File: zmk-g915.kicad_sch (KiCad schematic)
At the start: 43 parts, among them J3 Prog_conn, J5 Tag connect TC2030-CTX, SW2 Reset Switch, U3 nRF52840-QIAA-R/nRF52833-QIAA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, Y1 32MHz, Y2 32.768kHz

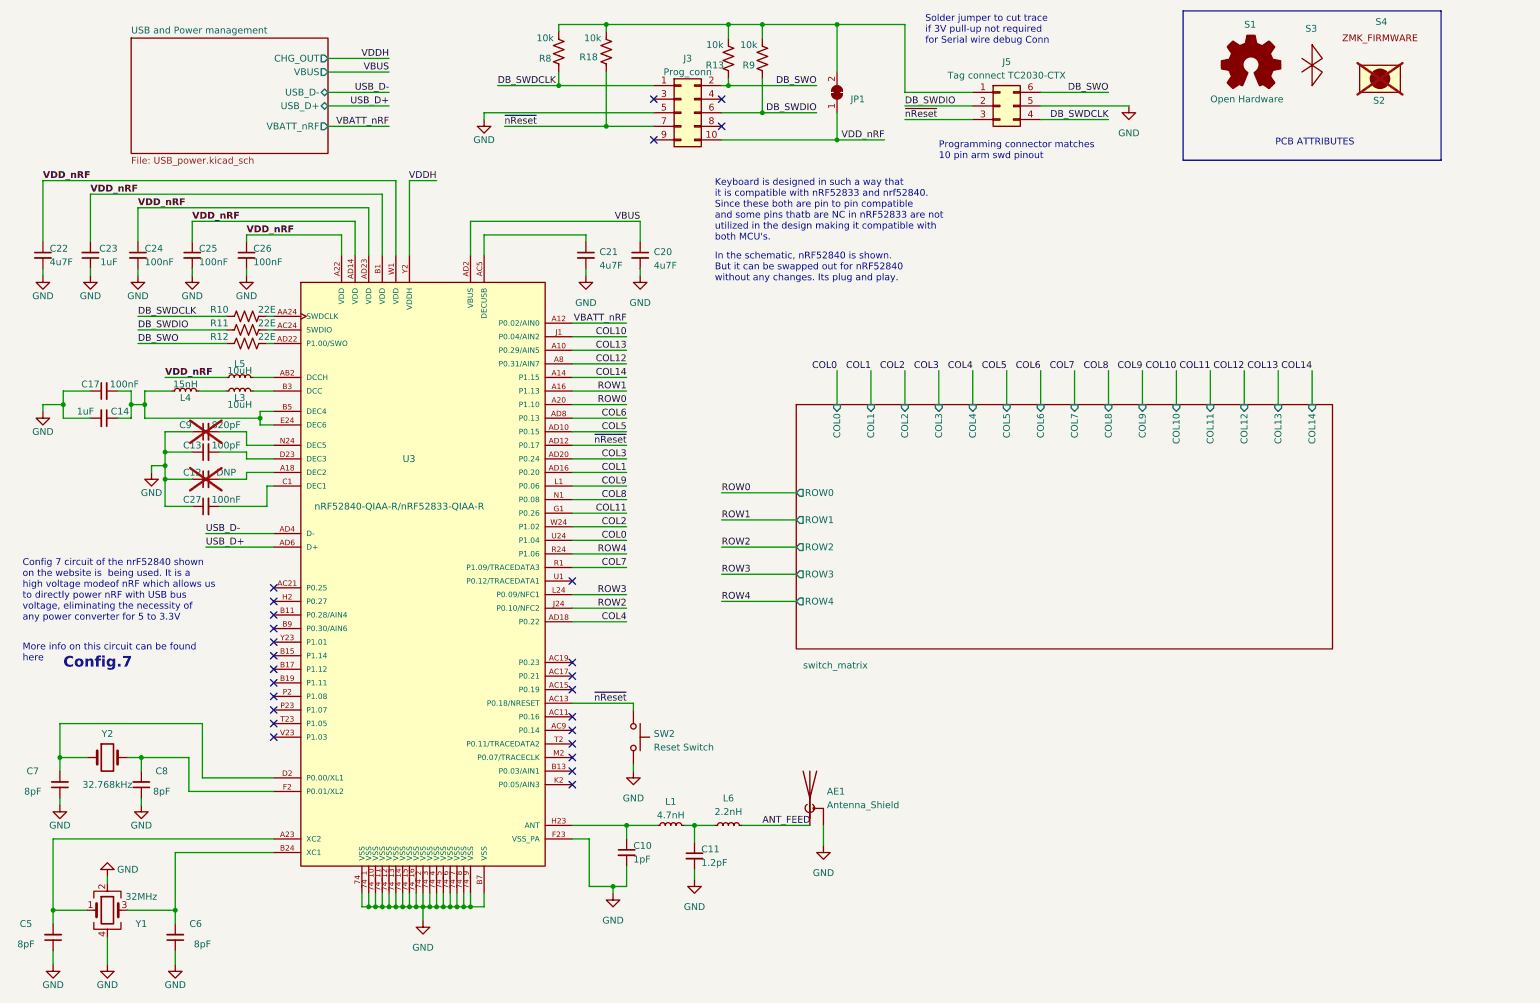
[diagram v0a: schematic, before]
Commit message: RGB and Keys added to sch
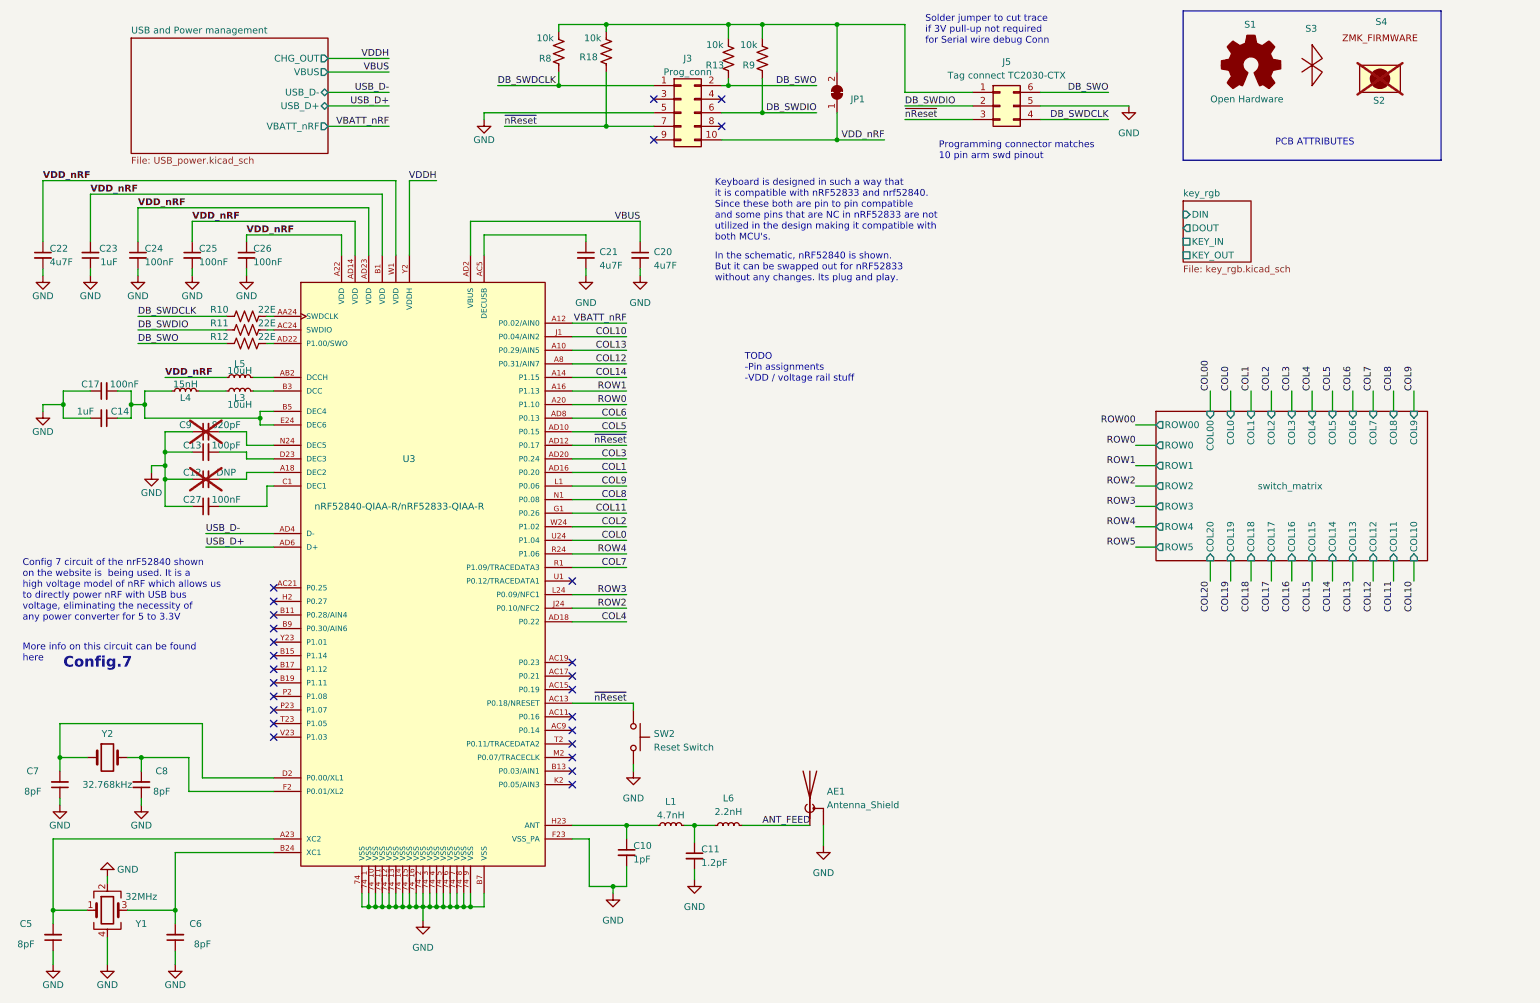
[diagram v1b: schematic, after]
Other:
- added sheet key_rgb (key_rgb.kicad_sch)
- sheet switch_matrix ports: added COL00, COL15, COL16, COL17, COL18, COL19, COL20, ROW00, ROW5; removed none
- note added: "Config 7 circuit of the nrF52840 shown on the website is being used. It is a high voltage model of nRF which allows us to directly power nRF with USB bus voltage, eliminating the necessity of any power converter for 5 to 3.3V"
- note added: "In the schematic, nRF52840 is shown. But it can be swapped out for nRF52833 without any changes. Its plug and play."
- note added: "Keyboard is designed in such a way that it is compatible with nRF52833 and nrf52840. Since these both are pin to pin compatible and some pins that are NC in nRF52833 are not utilized in the design making it compatible with both MCU's."
- note added: "TODO -Pin assignments -VDD / voltage rail stuff"
- note removed: "Config 7 circuit of the nrF52840 shown on the website is being used. It is a high voltage modeof nRF which allows us to directly power nRF with USB bus voltage, eliminating the necessity of any power converter for 5 to 3.3V"
- note removed: "In the schematic, nRF52840 is shown. But it can be swapped out for nRF52840 without any changes. Its plug and play."
- note removed: "Keyboard is designed in such a way that it is compatible with nRF52833 and nrf52840. Since these both are pin to pin compatible and some pins thatb are NC in nRF52833 are not utilized in the design making it compatible with both MCU's."

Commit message: Unified key sch pages
One large page is simpler in this case
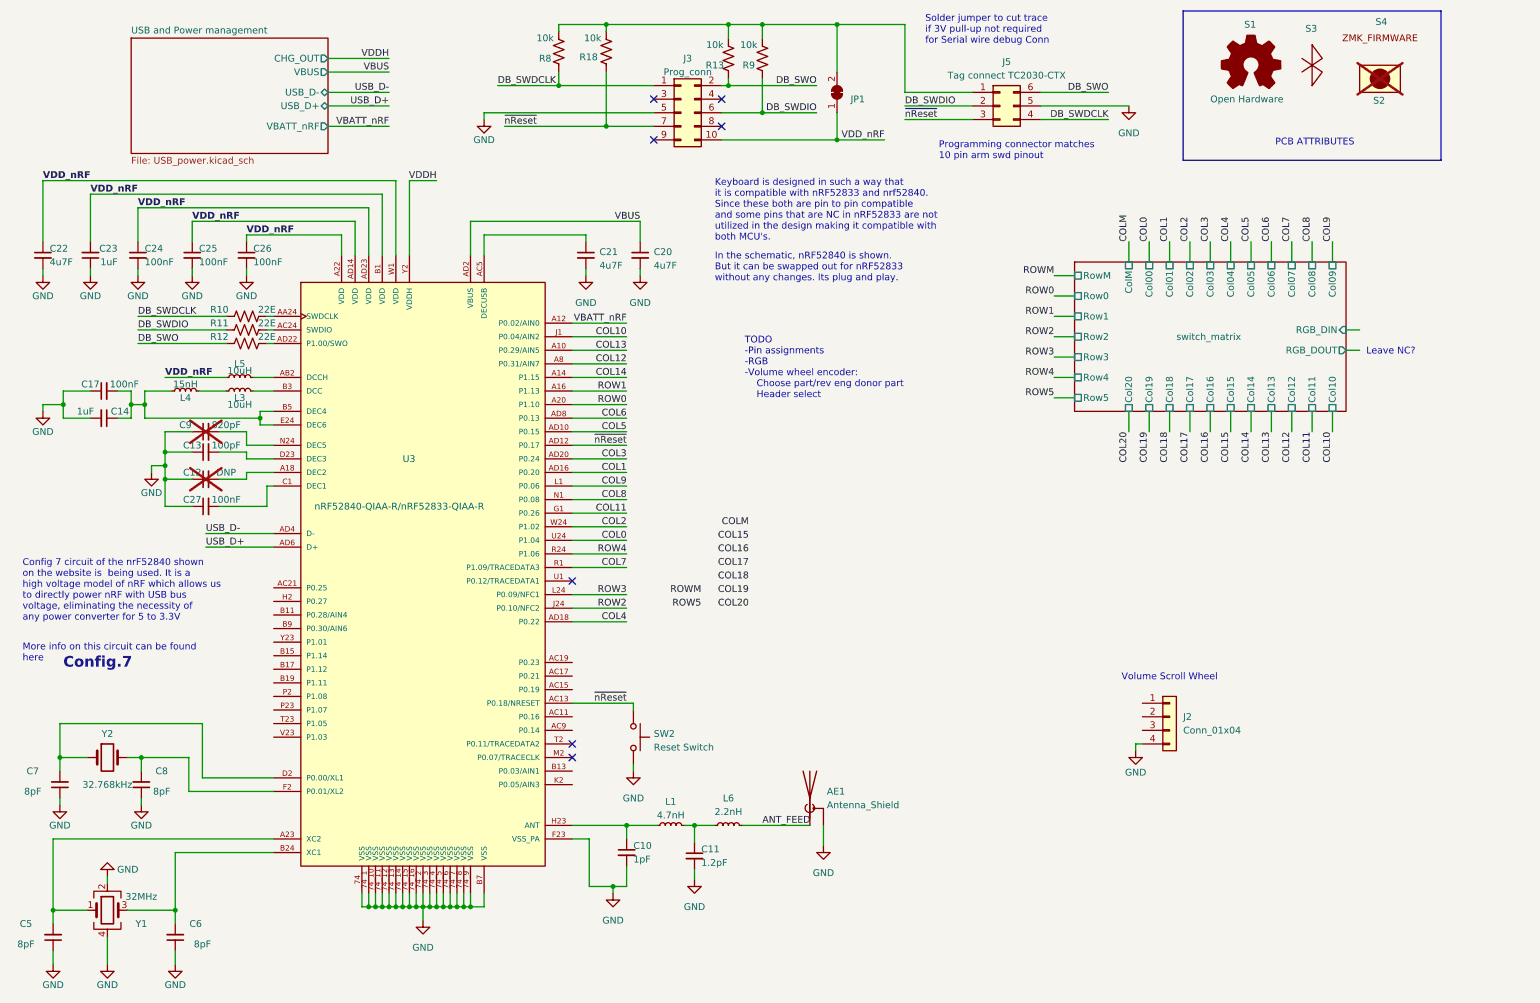
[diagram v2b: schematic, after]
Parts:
- added J2: Conn_01x04, symbol Connector_Generic:Conn_01x04
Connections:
- net GND: now also J2.4 (Pin_4)
- no-connect marks 26 -> 7
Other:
- removed sheet key_rgb
- sheet switch_matrix ports: added Col00, Col01, Col02, Col03, Col04, Col05, Col06, Col07, Col08, Col09, Col10, Col11, Col12, Col13, Col14, Col15, Col16, Col17, Col18, Col19, Col20, ColM, RGB_DIN, RGB_DOUT, Row0, Row1, Row2, Row3, Row4, Row5, RowM; removed COL0, COL00, COL1, COL10, COL11, COL12, COL13, COL14, COL15, COL16, COL17, COL18, COL19, COL2, COL20, COL3, COL4, COL5, COL6, COL7, COL8, COL9, ROW0, ROW00, ROW1, ROW2, ROW3, ROW4, ROW5
- note added: "Leave NC?"
- note added: "TODO -Pin assignments -RGB -Volume wheel encoder: Choose part/rev eng donor part Header select"
- note added: "Volume Scroll Wheel"
- note removed: "TODO -Pin assignments -VDD / voltage rail stuff"

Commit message: RGB LED level shifter. Various components
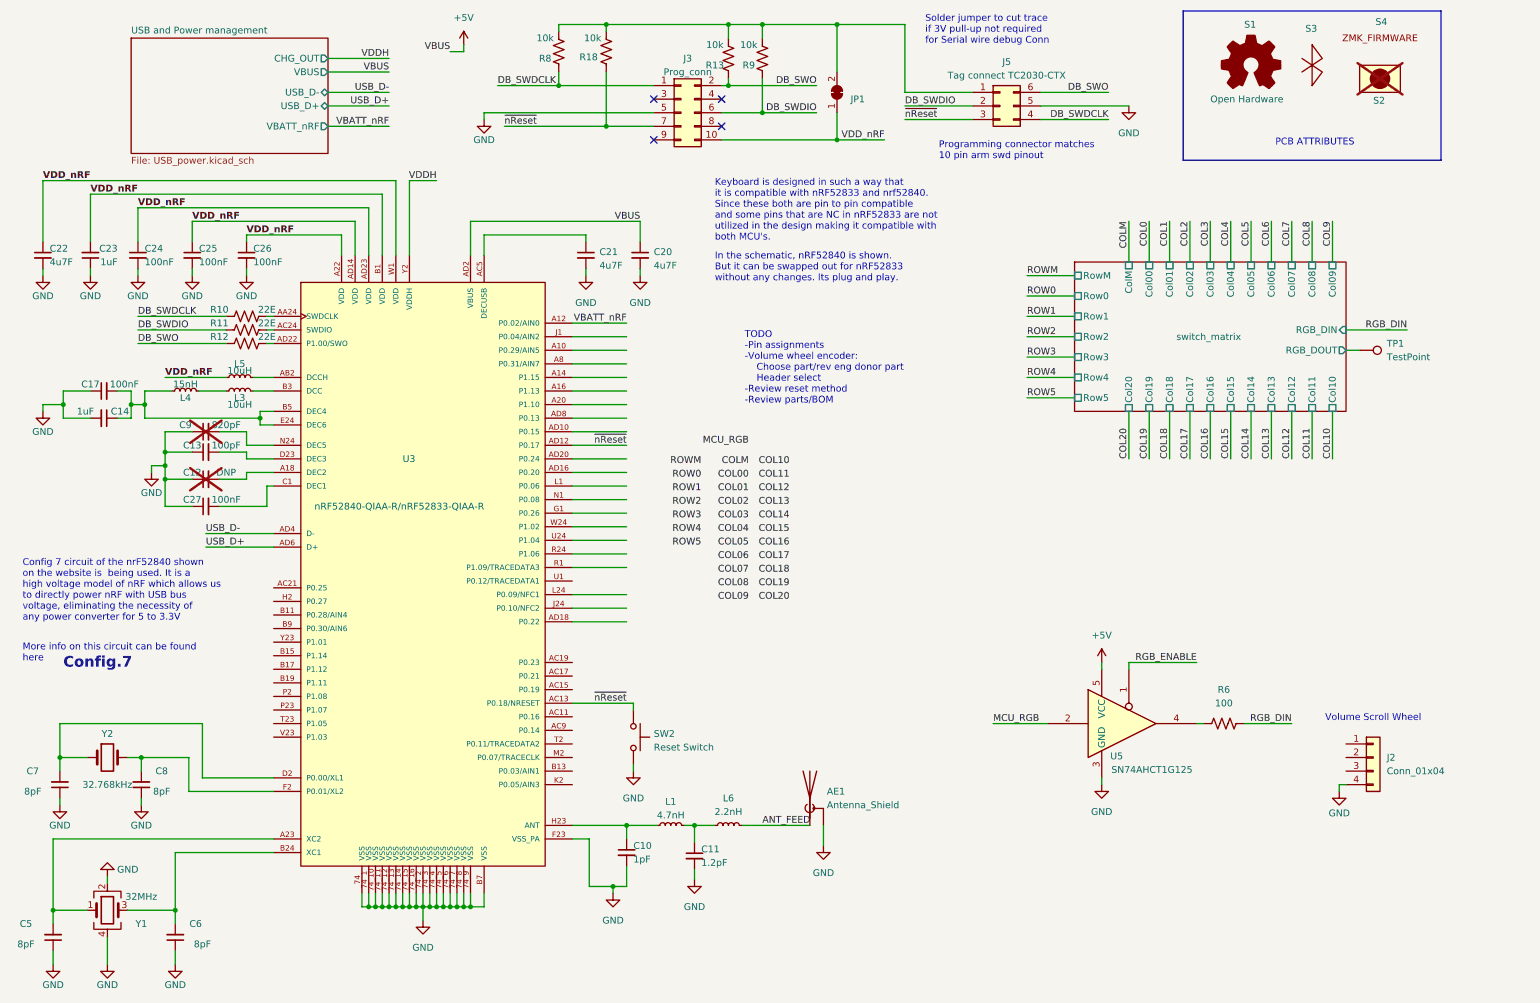
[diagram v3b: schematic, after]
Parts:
- added R6: 100, symbol Device:R_US
- added TP1: TestPoint, TestPoint:TestPoint_Pad_D1.5mm, symbol Connector:TestPoint
- added U5: SN74AHCT1G125, Package_TO_SOT_SMD:SOT-23-5, symbol 74xGxx:SN74LVC1G125DBV
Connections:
- net COL0: no longer U3.U24 (P1.04)
- net COL1: no longer U3.AD16 (P0.20)
- net COL10: no longer U3.J1 (P0.04/AIN2)
- net COL11: no longer U3.G1 (P0.26)
- net COL12: no longer U3.A8 (P0.31/AIN7)
- net COL13: no longer U3.A10 (P0.29/AIN5)
- net COL14: no longer U3.A14 (P1.15)
- net COL2: no longer U3.W24 (P1.02)
- net COL3: no longer U3.AD20 (P0.24)
- net COL4: no longer U3.AD18 (P0.22)
- net COL5: no longer U3.AD10 (P0.15)
- net COL6: no longer U3.AD8 (P0.13)
- net COL7: no longer U3.R1 (P1.09/TRACEDATA3)
- net COL8: no longer U3.N1 (P0.08)
- net COL9: no longer U3.L1 (P0.06)
- net GND: now also U5.3 (GND)
- net ROW0: no longer U3.A20 (P1.10)
- net ROW1: no longer U3.A16 (P1.13)
- net ROW2: no longer U3.J24 (P0.10/NFC2)
- net ROW3: no longer U3.L24 (P0.09/NFC1)
- net ROW4: no longer U3.R24 (P1.06)
- net switch_matrix/RGB_DOUT: now also TP1.1
- net VBUS renamed +5V
- net +5V: now also U5.5 (VCC)
- new net: R6.1, U5.4
- new net MCU_RGB: U5.2
- new net RGB_DIN: R6.2
- new net RGB_ENABLE: U5.1
- no-connect marks 7 -> 4
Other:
- note added: "TODO -Pin assignments -Volume wheel encoder: Choose part/rev eng donor part Header select -Review reset method -Review parts/BOM"
- note removed: "Leave NC?"
- note removed: "TODO -Pin assignments -RGB -Volume wheel encoder: Choose part/rev eng donor part Header select"
- moved on the sheet: J2

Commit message: Layout start. Add symbols to proj lib
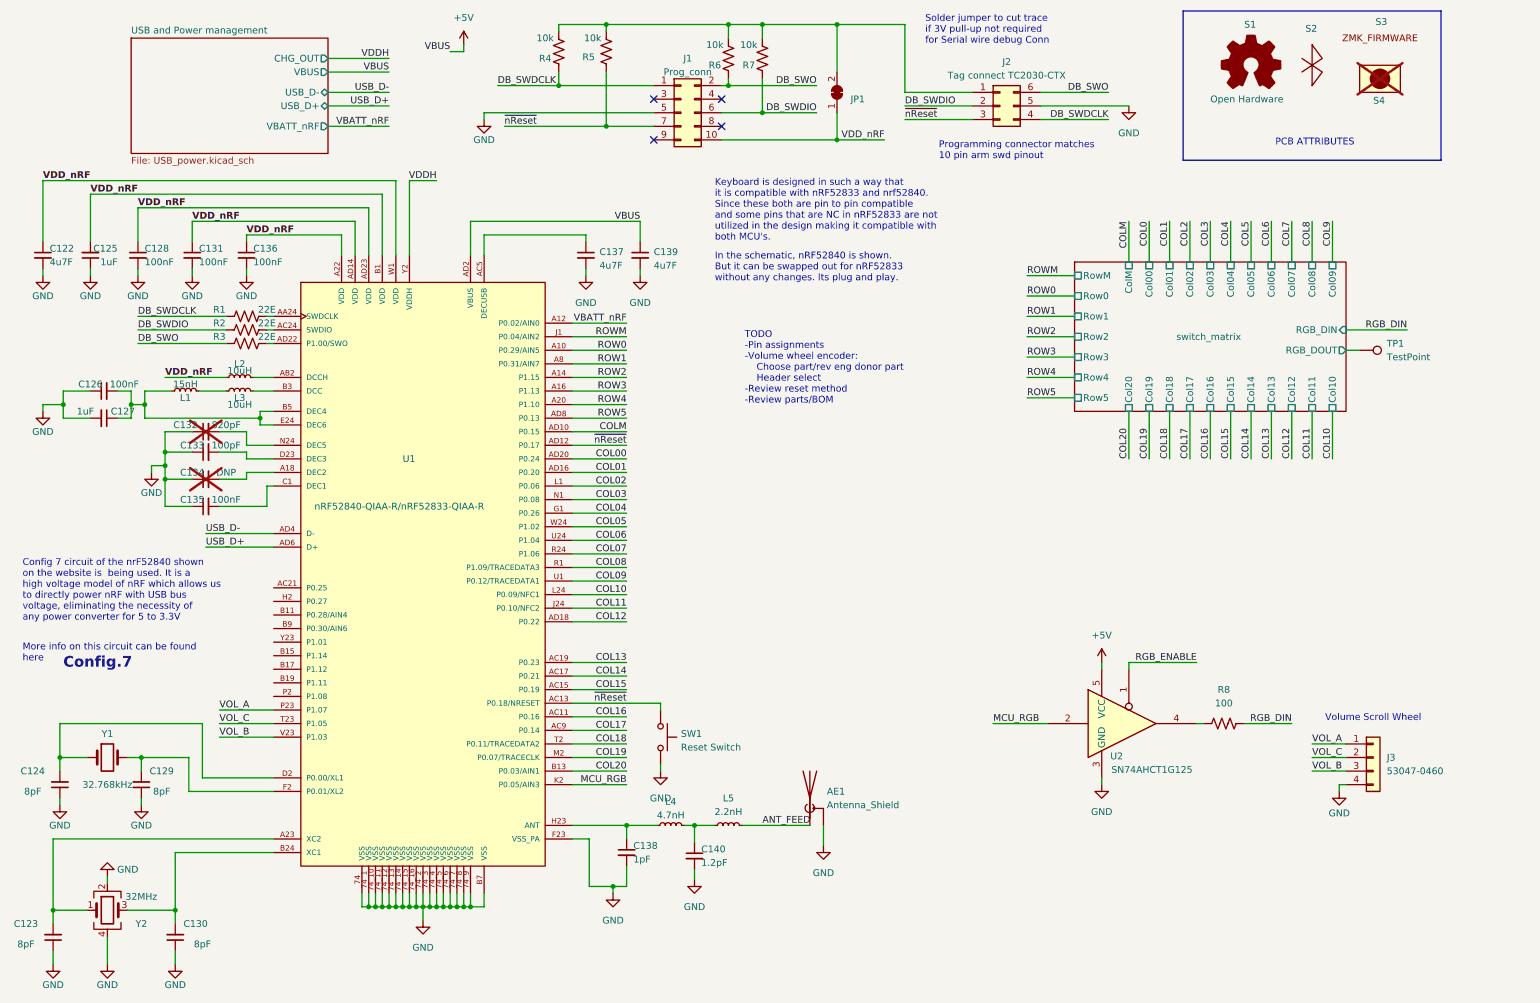
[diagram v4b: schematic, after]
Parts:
- J3: renamed from J2; value Conn_01x04 -> 53047-0460; footprint (none) -> Connector_Molex:Molex_PicoBlade_53048-0410_1x04_P1.25mm_Horizontal; symbol Connector_Generic:Conn_01x04 -> keyboard:Conn_01x04
- R8: renamed from R6; footprint (none) -> Resistor_SMD:R_0402_1005Metric; symbol Device:R_US -> keyboard:R_US
- U2: renamed from U5; symbol 74xGxx:SN74LVC1G125DBV -> keyboard:74LVC1G125
- renumbered C22 to C122, C5 to C123, C7 to C124, C23 to C125, C17 to C126, C14 to C127, C24 to C128, C8 to C129, C6 to C130, C25 to C131, C9 to C132, C13 to C133, C12 to C134, C27 to C135, C26 to C136, C21 to C137, C10 to C138, C20 to C139, C11 to C140, J3 to J1, J5 to J2, L4 to L1, L5 to L2, L1 to L4, L6 to L5, R10 to R1, R11 to R2, R12 to R3, R8 to R4, R18 to R5, R13 to R6, R9 to R7, S3 to S2, S4 to S3, S2 to S4, SW2 to SW1, U3 to U1, Y2 to Y1, Y1 to Y2
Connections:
- net COL00: now also U1.AD20 (P0.24)
- net COL01: now also U1.AD16 (P0.20)
- net COL02: now also U1.L1 (P0.06)
- net COL03: now also U1.N1 (P0.08)
- net COL04: now also U1.G1 (P0.26)
- net COL05: now also U1.W24 (P1.02)
- net COL06: now also U1.U24 (P1.04)
- net COL07: now also U1.R24 (P1.06)
- net COL08: now also U1.R1 (P1.09/TRACEDATA3)
- net COL09: now also U1.U1 (P0.12/TRACEDATA1)
- net COL10: now also U1.L24 (P0.09/NFC1)
- net COL11: now also U1.J24 (P0.10/NFC2)
- net COL12: now also U1.AD18 (P0.22)
- net COL13: now also U1.AC19 (P0.23)
- net COL14: now also U1.AC17 (P0.21)
- net COL15: now also U1.AC15 (P0.19)
- net COL16: now also U1.AC11 (P0.16)
- net COL17: now also U1.AC9 (P0.14)
- net COL18: now also U1.T2 (P0.11/TRACEDATA2)
- net COL19: now also U1.M2 (P0.07/TRACECLK)
- net COL20: now also U1.B13 (P0.03/AIN1)
- net COLM: now also U1.AD10 (P0.15)
- net MCU_RGB: now also U1.K2 (P0.05/AIN3)
- net ROW0: now also U1.A10 (P0.29/AIN5)
- net ROW1: now also U1.A8 (P0.31/AIN7)
- net ROW2: now also U1.A14 (P1.15)
- net ROW3: now also U1.A16 (P1.13)
- net ROW4: now also U1.A20 (P1.10)
- net ROW5: now also U1.AD8 (P0.13)
- net ROWM: now also U1.J1 (P0.04/AIN2)
- net VOL_A: now reaches J3.1 (Pin_1)
- net VOL_A: now also U1.P23 (P1.07)
- net VOL_C: now reaches J3.2 (Pin_2)
- net VOL_C: now also U1.T23 (P1.05)
- net VOL_B: now reaches J3.3 (Pin_3)
- net VOL_B: now also U1.V23 (P1.03)
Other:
- moved on the sheet: SW1
